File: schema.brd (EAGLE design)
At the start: 130 x 130 mm, 19 parts, among them IC1 RT9011-CMGJ6, IC2 SX1308, J1 FH12-24S-0.5SH(55), U1 ESP-32S, X2 C-GRID-02-70543

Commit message: Added new components
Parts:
- added J2: C10418, water-lib:C10418
- added U2: CH340ESMD, water-lib:MSOP10
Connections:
- new net D+: J2.3, U2.1
- new net D-: J2.2, U2.2
- new net N$10: J2.4
- new net N$11: J2.MH1, J2.MH2, J2.MH3, J2.MH4
- new net V3: U2.10
- new net VCC: U2.7
- net +5V: now also J2.1
- net GND: now also J2.5, U2.3
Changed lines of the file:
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@@
 <?xml version="1.0" encoding="utf-8"?>
 <!DOCTYPE eagle SYSTEM "eagle.dtd">
-<eagle version="9.4.2">
+<eagle version="9.5.0">
 <drawing>
 <settings>
@@
 <attribute name="VALUE" x="13.7575" y="96.7825" size="0.8128" layer="27" ratio="10"/>
 </element>
+<element name="U2" library="water-lib" package="MSOP10" package3d_urn="urn:adsk.eagle:package:3661278/1" value="CH340ESMD" x="37" y="34" smashed="yes">
+<attribute name="NAME" x="34.46" y="36.032" size="1.27" layer="25" ratio="10"/>
+</element>
+<element name="J2" library="water-lib" package="C10418" value="C10418" x="1" y="46" smashed="yes" rot="R90">
+<attribute name="DESCRIPTION" value="USB Connectors SMD RoHS" x="1" y="46" size="1.778" layer="27" rot="R90" display="off"/>
+<attribute name="HEIGHT" value="3.15mm" x="1" y="46" size="1.778" layer="27" rot="R90" display="off"/>
+<attribute name="MANUFACTURER_NAME" value="Jing Extension of the Electronic Co." x="1" y="46" size="1.778" layer="27" rot="R90" display="off"/>
+<attribute name="MANUFACTURER_PART_NUMBER" value="C10418" x="1" y="46" size="1.778" layer="27" rot="R90" display="off"/>
+<attribute name="MOUSER_PART_NUMBER" value="" x="1" y="46" size="1.778" layer="27" rot="R90" display="off"/>
+<attribute name="MOUSER_PRICE-STOCK" value="" x="1" y="46" size="1.778" layer="27" rot="R90" display="off"/>
+<attribute name="NAME" x="1.4" y="46" size="1.27" layer="25" rot="R90" align="center"/>
+<attribute name="RS_PART_NUMBER" value="" x="1" y="46" size="1.778" layer="27" rot="R90" display="off"/>
+<attribute name="RS_PRICE-STOCK" value="" x="1" y="46" size="1.778" layer="27" rot="R90" display="off"/>
+<attribute name="VALUE" x="1.4" y="46" size="1.27" layer="27" rot="R90" align="center"/>
+</element>
 </elements>
 <signals>
@@
 <vertex x="-13" y="-18"/>
 </polygon>
+<contactref element="U2" pad="3"/>
+<contactref element="J2" pad="5"/>
+<wire x1="45.89" y1="102.24" x2="64.39" y2="102.24" width="0" layer="19" extent="1-1"/>
+<wire x1="34.1512" y1="97.5494" x2="45.89" y2="102.24" width="0" layer="19" extent="1-1"/>
+<wire x1="27.6488" y1="97.5494" x2="34.1512" y2="97.5494" width="0" layer="19" extent="1-1"/>
+<wire x1="15.98" y1="93.29" x2="27.6488" y2="97.5494" width="0" layer="19" extent="1-1"/>
+<wire x1="49.44" y1="83.99" x2="45.89" y2="102.24" width="0" layer="19" extent="1-1"/>
+<wire x1="36.82" y1="76.8" x2="49.44" y2="83.99" width="0" layer="19" extent="1-1"/>
+<wire x1="28.69" y1="69.18" x2="36.82" y2="76.8" width="0" layer="19" extent="1-1"/>
+<wire x1="18.66" y1="61.09" x2="28.69" y2="69.18" width="0" layer="19" extent="1-1"/>
+<wire x1="15.92" y1="64.49" x2="18.66" y2="61.09" width="0" layer="19" extent="1-1"/>
+<wire x1="10.76" y1="63.88" x2="15.92" y2="64.49" width="0" layer="19" extent="1-1"/>
+<wire x1="6.59" y1="58.69" x2="10.76" y2="63.88" width="0" layer="19" extent="1-1"/>
+<wire x1="25.27" y1="52.8" x2="18.66" y2="61.09" width="0" layer="19" extent="1-1"/>
+<wire x1="29.04" y1="41.18" x2="25.27" y2="52.8" width="0" layer="19" extent="1-1"/>
+<wire x1="34.8869" y1="34" x2="29.04" y2="41.18" width="0" layer="19" extent="1-1"/>
+<wire x1="4" y1="44.7" x2="34.8869" y2="34" width="0" layer="19" extent="1-1"/>
 </signal>
 <signal name="N$1">
@@
 <wire x1="18.6" y1="65.9" x2="18.6" y2="63.05" width="0.1524" layer="1"/>
 <wire x1="18.6" y1="63.05" x2="18.66" y2="62.99" width="0.1524" layer="1"/>
+<contactref element="J2" pad="1"/>
+<wire x1="4" y1="47.3" x2="12.96" y2="58.8" width="0" layer="19" extent="1-1"/>
+</signal>
+<signal name="VCC">
+<contactref element="U2" pad="7"/>
+</signal>
+<signal name="V3">
+<contactref element="U2" pad="10"/>
+</signal>
+<signal name="D+">
+<contactref element="U2" pad="1"/>
+<contactref element="J2" pad="3"/>
+<wire x1="4" y1="46" x2="34.8869" y2="35" width="0" layer="19" extent="1-1"/>
+</signal>
+<signal name="D-">
+<contactref element="U2" pad="2"/>
+<contactref element="J2" pad="2"/>
+<wire x1="4" y1="46.65" x2="34.8869" y2="34.5" width="0" layer="19" extent="1-1"/>
+</signal>
+<signal name="N$10">
+<contactref element="J2" pad="4"/>
+</signal>
+<signal name="N$11">
+<contactref element="J2" pad="MH1"/>
+<contactref element="J2" pad="MH3"/>
+<contactref element="J2" pad="MH4"/>
+<contactref element="J2" pad="MH2"/>
+<wire x1="3.48" y1="43.575" x2="0.8" y2="42.375" width="0" layer="19" extent="1-1"/>
+<wire x1="3.48" y1="48.425" x2="3.48" y2="43.575" width="0" layer="19" extent="1-1"/>
+<wire x1="0.8" y1="49.625" x2="3.48" y2="48.425" width="0" layer="19" extent="1-1"/>
 </signal>
 </signals>

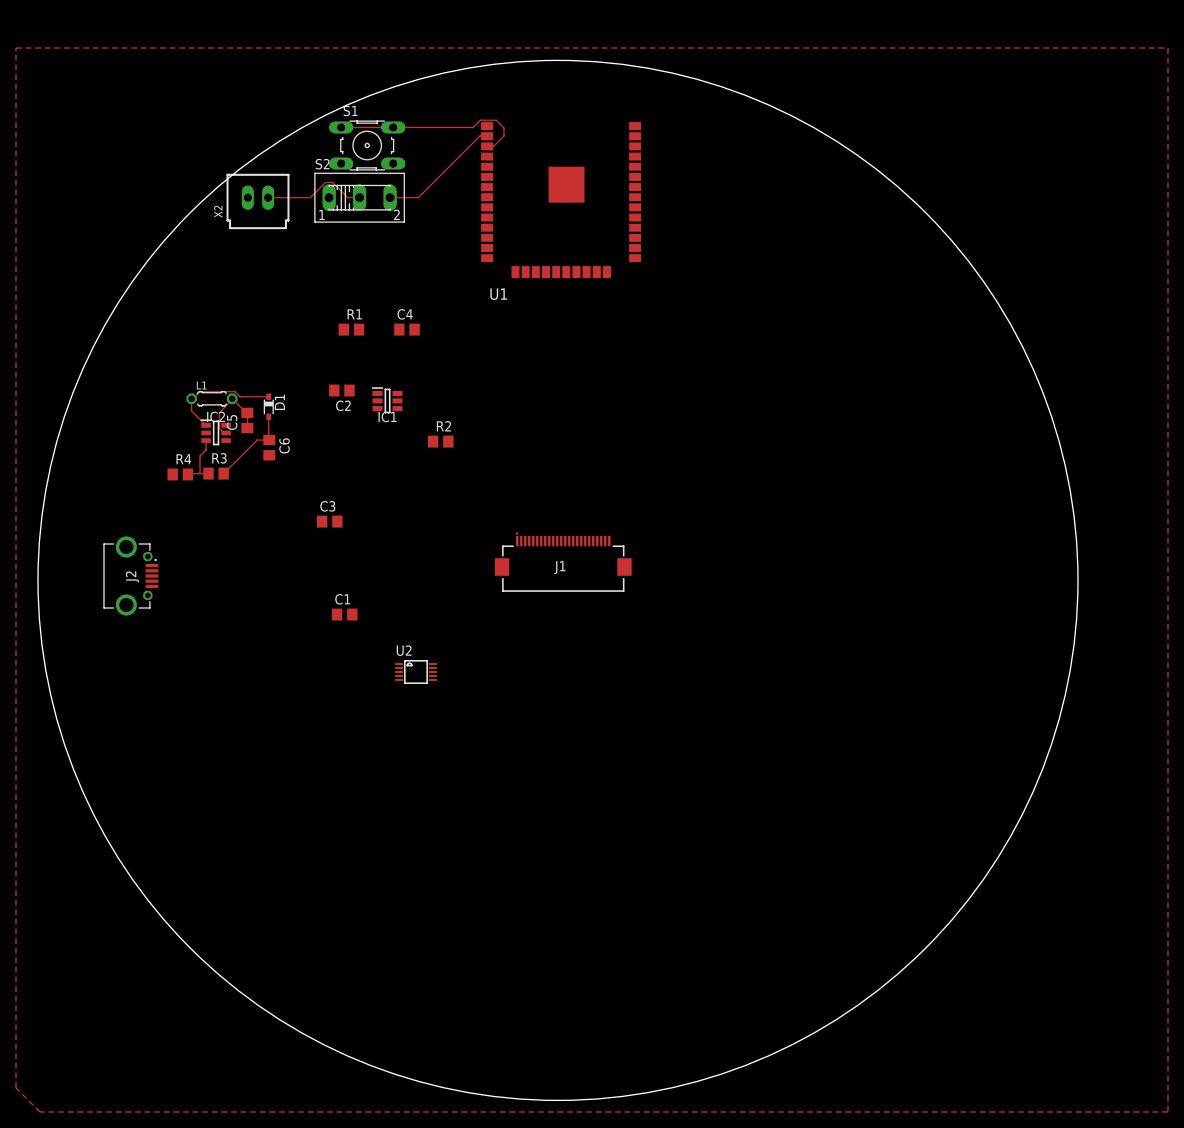
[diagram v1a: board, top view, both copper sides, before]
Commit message: Added USB-Serial to main design
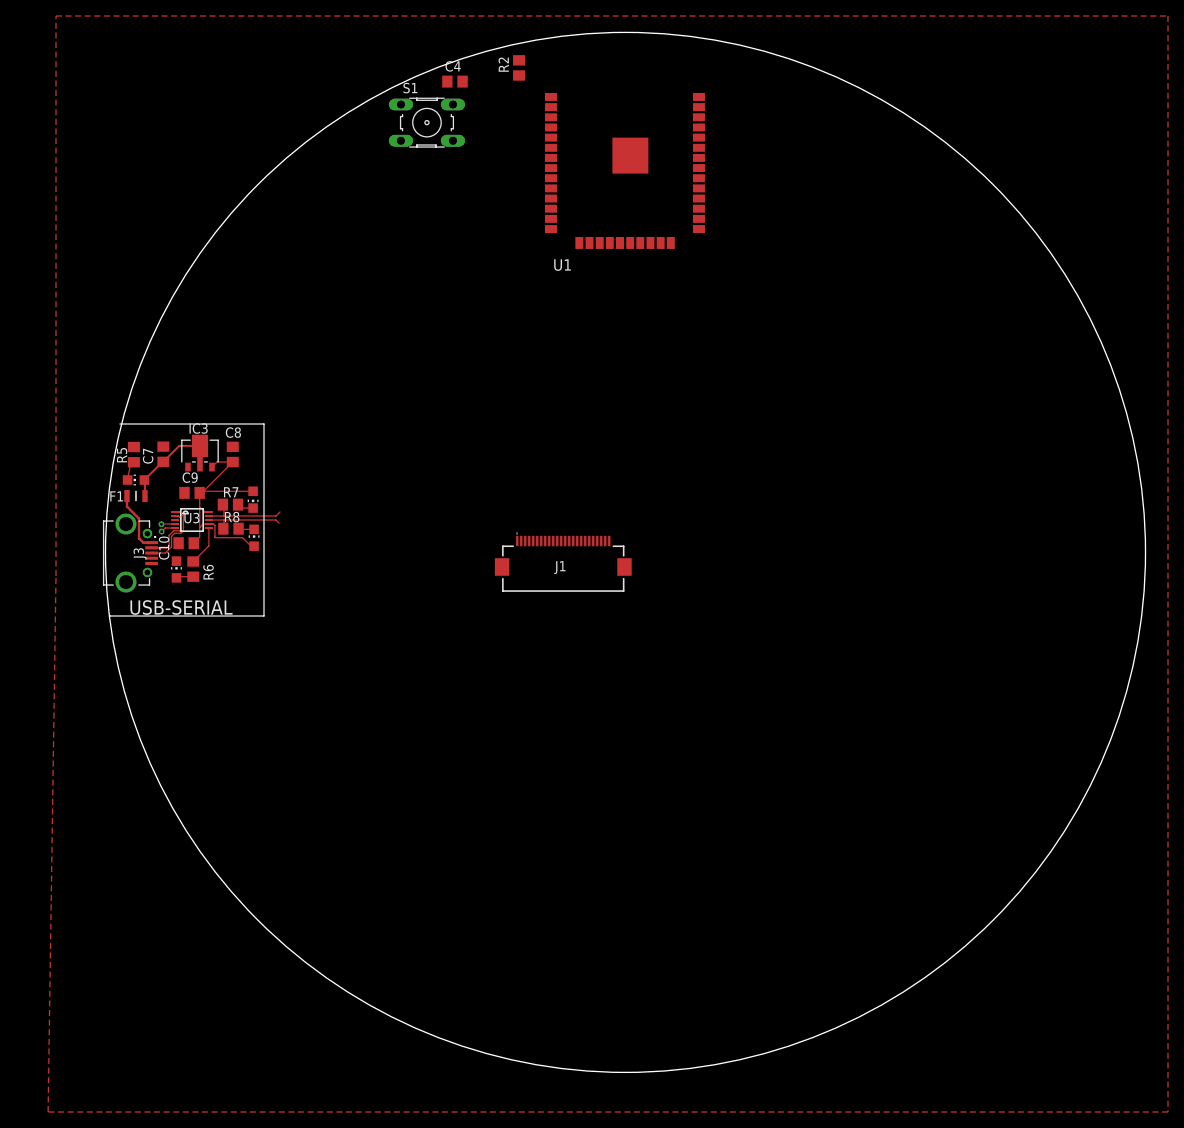
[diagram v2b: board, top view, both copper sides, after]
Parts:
- removed C1, C2, C3: 0.1uF, rcl:C0805
- removed C5, C6: 22uF, rcl:C0805
- removed D1: BAT60J, diode:SOD323_ST
- removed IC1: RT9011-CMGJ6, water-lib:SOT94P280X100-6N
- removed IC2: SX1308, water-lib:SOT95P280X145-6N
- removed J2: C10418, water-lib:C10418
- removed L1: 22uH, rcl:0204/5
- removed R1: 1k, rcl:R0805
- removed R3: 10k, rcl:R0805
- removed R4: 1363, rcl:R0805
- removed S2: (no value), switch:255SB
- removed U2: CH340ESMD, water-lib:MSOP10
- removed X2: C-GRID-02-70543, con-molex:70543-02
- added C10, C9: .1uF, rcl:C0805
- added C7, C8: 10uF, rcl:C0805
- added F1: SMD0805-020-16V, water-lib:FUSC2114X100N
- added IC3: HT7333, water-lib:SOT-89
- added J3: C10418, water-lib:C10418
- added LED1, LED2, LED3, LED4: (no value), led:CHIP-LED0805
- added R5: 2k, rcl:R0805
- added R6, R7, R8: 1K5, rcl:R0805
- added U3: CH340ESMD, water-lib:MSOP10
- moved R2 47.7 mm to (49.9, 109.5), turned to 90 degrees
- moved C4 31.6 mm to (41.9, 107.8)
- moved U1 8.77 mm to (63.1, 98.9)
- moved S1 8.00 mm to (38.4, 102.7)
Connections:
- removed net +1V2: C2.2, IC1.1
- removed net +2V8: C3.2, IC1.6
- removed net +5V: C6.1, D1.A, J2.1, R3.2
- removed net CAM_PWR: R1.1, U1.7
- removed net D+: J2.3, U2.1
- removed net D-: J2.2, U2.2
- removed net N$1: IC1.3, IC1.4, R1.2
- removed net N$10: J2.4
- removed net N$11: J2.MH1, J2.MH2, J2.MH3, J2.MH4
- removed net N$2: U1.GND
- removed net N$3: S2.2, X2.2
- removed net N$4: D1.C, IC2.1, L1.1
- removed net N$5: IC2.3, R3.1, R4.2
- removed net V3: U2.10
- removed net VCC: U2.7
- new net +5V1: C7.1, F1.2, IC3.3, IC3.4, LED1.A
- new net 3V3: C10.1, C8.1, C9.2, IC3.1, LED3.A, LED4.A, U3.10, U3.7
- new net 5V-USB: F1.1, J3.1
- new net CTS: U3.5
- new net D+1: J3.3, U3.1
- new net D-1: J3.2, U3.2
- new net MH: J3.MH1, J3.MH2, J3.MH3, J3.MH4
- new net N$12: LED3.C, R7.2
- new net N$13: LED4.C, R8.1
- new net N$7: LED1.C, R5.2
- new net N$8: R6.1, U3.6
- new net N$9: LED2.A, R6.2
- new net NC1: J3.4
- new net RTS: U3.4
- new net RX: R7.1, U1.35, U3.9
- new net TX: R8.2, U1.34, U3.8
- net +3V3: no longer C1.1, C5.2, IC1.5, IC2.4, IC2.5, L1.2, S2.3
- net GND: now also C10.2, C7.2, C8.2, C9.1, IC3.2, J3.5, LED2.C, R5.1, U1.GND, U3.3; no longer C1.2, C2.1, C3.1, C5.1, C6.2, IC2.2, J2.5, R4.1, U2.3, X2.1
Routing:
- net 3V3: track 0.00 -> 32.4 mm
- net +3V3: track 25.6 -> 0.04 mm
- net EN: track 24.8 -> 0.00 mm
- net N$4: track 14.8 -> 0.00 mm
- net +5V1: track 0.00 -> 13.0 mm
- net N$3: track 13.0 -> 0.00 mm
- net RX: track 0.00 -> 10.6 mm
- net +5V: track 10.4 -> 0.00 mm
- net TX: track 0.00 -> 10.1 mm
- net D+1: track 0.00 -> 8.96 mm
- net 5V-USB: track 0.00 -> 7.71 mm
- net D-1: track 0.00 -> 7.67 mm
- net N$5: track 7.06 -> 0.00 mm
- net N$8: track 0.00 -> 5.00 mm
- net N$7: track 0.00 -> 2.45 mm
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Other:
- board text added: "USB-SERIAL"
